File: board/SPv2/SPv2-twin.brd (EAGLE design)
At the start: 128.4 x 22.9 mm, 70 parts, among them IC1 S34ML0XG1, IC2 F5508, IC3 S34ML0XG1, IC4 74LS14D, IC5 F5508, IC6 74LS14D, Q1 12MHz, Q2 12MHz

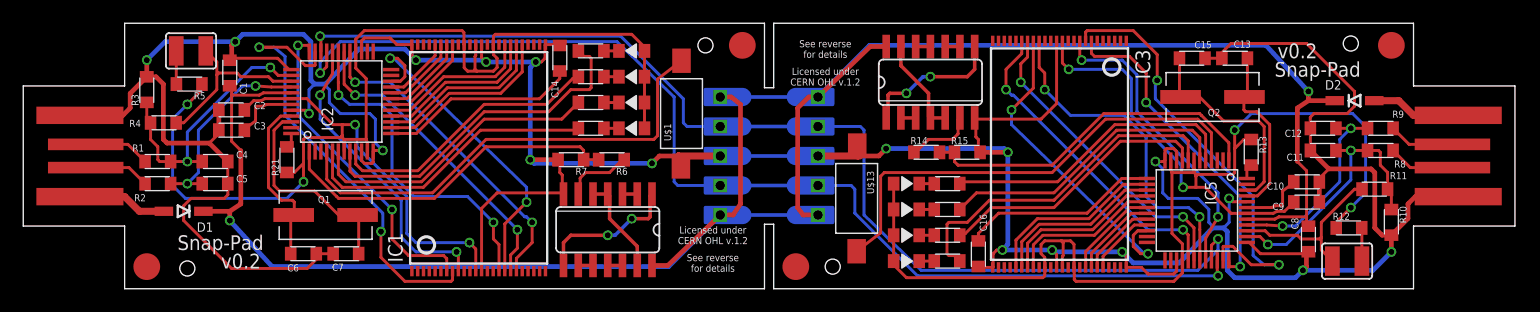
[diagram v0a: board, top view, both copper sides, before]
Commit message: silks cleaned up on twin
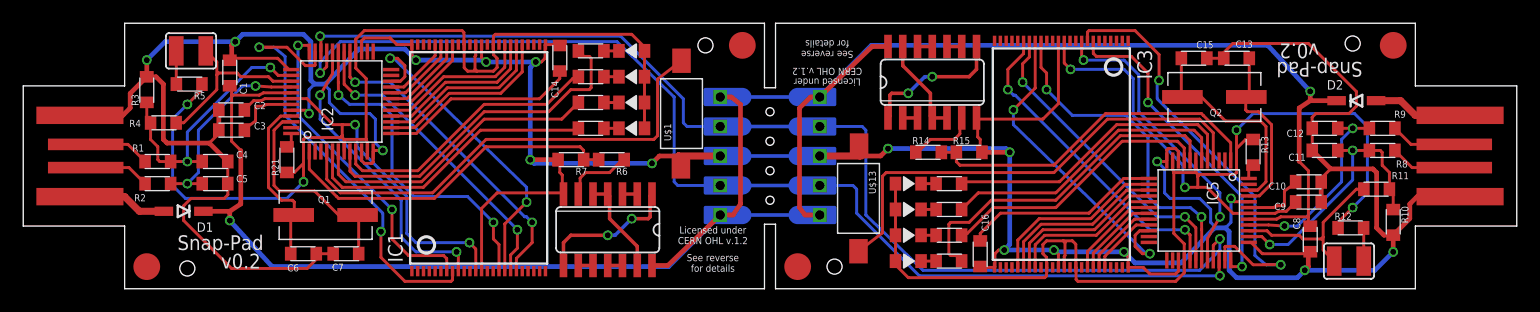
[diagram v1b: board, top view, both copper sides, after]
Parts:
- moved C10 0.16 mm to (110.6, 9.21)
- moved C15 0.16 mm to (100.8, 19.8)
- moved C9 0.16 mm to (110.6, 7.46)
- moved R14 0.16 mm to (77.9, 11.7)
- moved C11 0.16 mm to (112.1, 11.9)
- moved C12 0.16 mm to (112.1, 13.8)
- moved C13 0.16 mm to (104.5, 19.8)
- moved C16 0.16 mm to (82.4, 3.02)
- moved C8 0.16 mm to (110.8, 4.29)
- moved D2 0.16 mm to (114.8, 16.2)
- moved IC3 0.16 mm to (89.4, 11.6)
- moved IC5 0.16 mm to (101.2, 6.74)
- moved IC6 0.16 mm to (78.3, 17.8)
- moved JP2 0.16 mm to (123.5, 11.4)
- moved Q2 0.16 mm to (102.6, 16.5)
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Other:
- board size 128.4 x 22.9 mm -> 128.6 x 22.9 mm
